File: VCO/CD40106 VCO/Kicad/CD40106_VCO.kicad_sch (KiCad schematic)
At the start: 48 parts

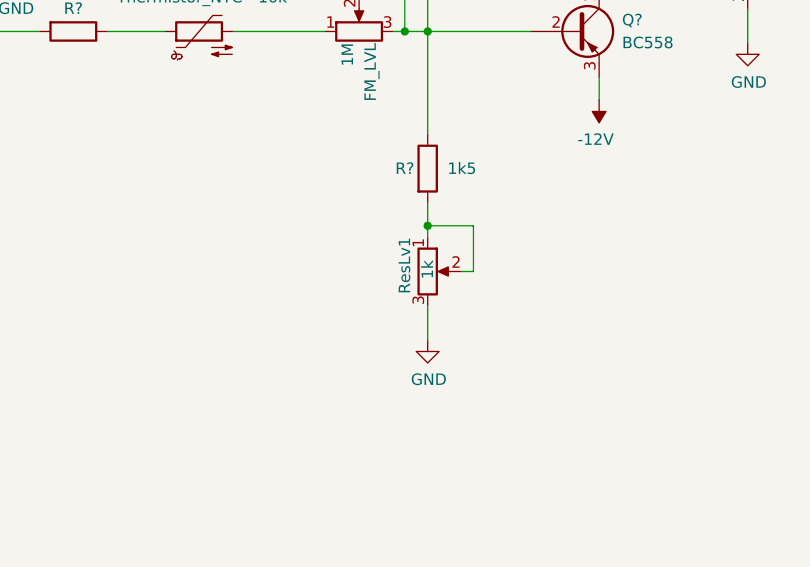
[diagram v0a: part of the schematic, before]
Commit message: Schem finished (no 2nd board added yet)
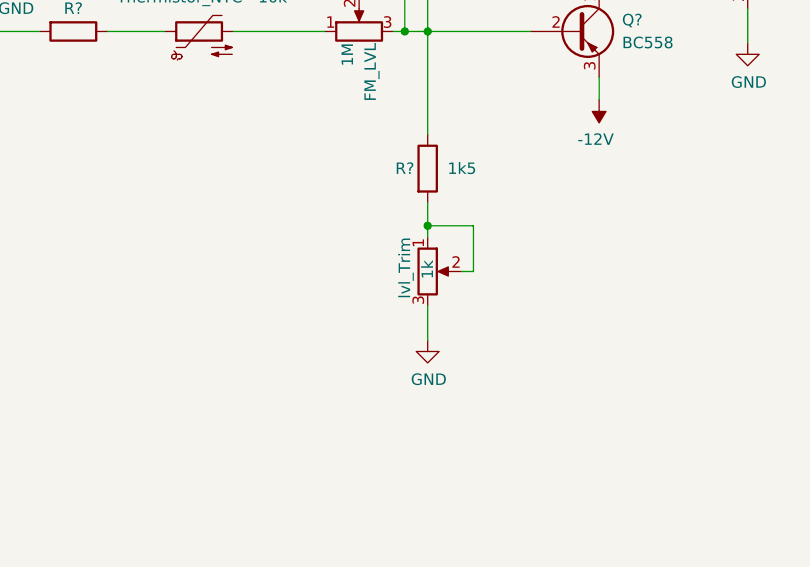
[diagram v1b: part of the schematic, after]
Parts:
- renumbered ResLv1 to lvl_Trim

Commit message: added connectors between boards
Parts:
- added H? (x2): SpacerHoles, MountingHole:MountingHole_3.2mm_M3, symbol Mechanical:MountingHole
- added J? (x2): Conn_01x08_Female, Connector_PinSocket_2.54mm:PinSocket_1x08_P2.54mm_Vertical, symbol Connector:Conn_01x08_Female
- added J? (x2): Conn_01x08_Male, Connector_PinHeader_2.54mm:PinHeader_1x08_P2.54mm_Vertical, symbol Connector:Conn_01x08_Male
- J1: renamed from J?; value 1V/OCT -> 1V/Oct
- J4: renamed from J?; value SAW -> Saw
- J5: renamed from J?; value SQUARE -> Square
- gave numbers to parts that had none: 28
- renumbered COARSE to Coarse, D6 to D1, FM_LVL to FM_LVL1, PWM to PWM1, PWM_CV_LVL to PWM_CV_LVL1, R18 to R1, R17 to R2, R15 to R4
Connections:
- net +12V: now also J?.2 (Pin_2), J?.2 (Pin_2)
- net -12V: now also J?.1 (Pin_1), J?.1 (Pin_1)
- net GND: now also J?.1 (Pin_1), J?.1 (Pin_1), J?.2 (Pin_2), J?.2 (Pin_2), J?.8 (Pin_8), J?.8 (Pin_8), J?.8 (Pin_8), J?.8 (Pin_8)
- net Coarse: now reaches Coarse.2, R4.2
- net Coarse: now also J?.3 (Pin_3), J?.3 (Pin_3)
- net at FM_LVL1.1: now also J2.T; no longer TH4.2
- net at Q1.2 (B), R8.1, TH1.2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: now also TH4.2; no longer FM_LVL1.2, FM_LVL1.3
- net Square out: now reaches J5.T, U1.13 (-), U1.14
- net Square out: now also J?.6 (Pin_6), J?.6 (Pin_6)
- net 1V/oct: now reaches J1.T, R6.2
- net 1V/oct: now also J?.7 (Pin_7), J?.7 (Pin_7)
- net PWM: now reaches PWM1.2, R10.2
- net PWM: now also J?.7 (Pin_7), J?.7 (Pin_7)
- net Saw out: now reaches J4.T, R18.1
- net Saw out: now also J?.5 (Pin_5), J?.5 (Pin_5)
- net PWM CV: now reaches PWM_CV_LVL1.3, R12.2
- net PWM CV: now also PWM_CV_LVL1.2, J?.5 (Pin_5), J?.5 (Pin_5)
- net Fm: now reaches R7.2
- net Fm: now also FM_LVL1.2, FM_LVL1.3, J?.6 (Pin_6), J?.6 (Pin_6); no longer J2.T
- net Fine: now reaches Fine.2, R5.2
- net Fine: now also J?.4 (Pin_4), J?.4 (Pin_4)
- new net Sine Out: J?.4 (Pin_4), J?.4 (Pin_4)
- new net Tri Out: J?.3 (Pin_3), J?.3 (Pin_3)
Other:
- moved on the sheet: Coarse, FM_LVL1, Fine, J1, J2, J3, J4, J5, PWM1, PWM_CV_LVL1, R1, R10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
